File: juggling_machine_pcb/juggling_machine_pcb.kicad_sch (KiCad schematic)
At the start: 16 parts, among them J1 Conn_01x08, J10 Screw_Terminal_01x04, J11 Screw_Terminal_01x04, J2 Conn_01x08, J3 Conn_01x08, J4 Conn_01x08, J5 servo 1, J6 servo 2, J7 24v input, J8 5v input, J9 24v out for input to buck

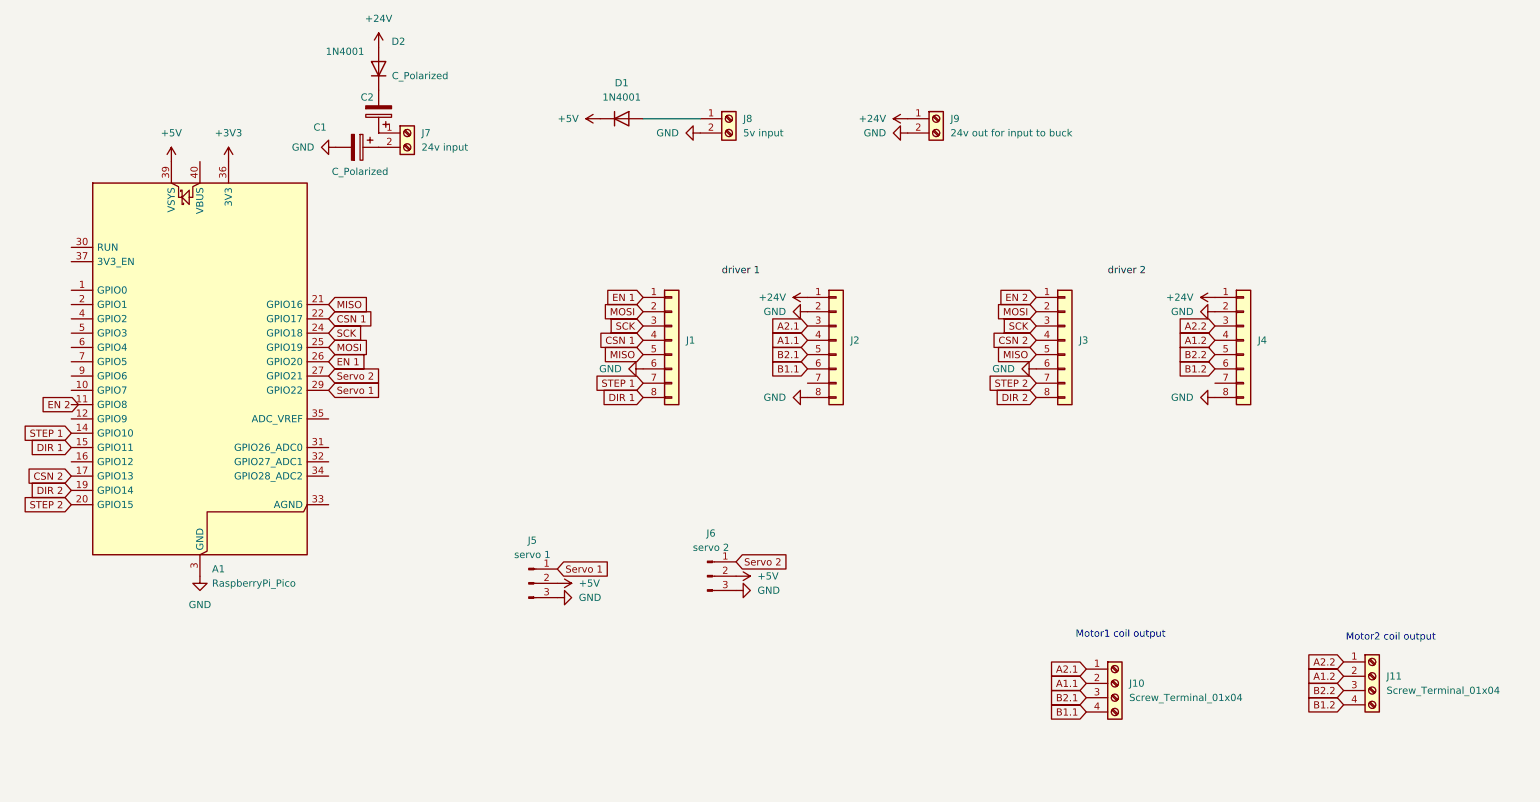
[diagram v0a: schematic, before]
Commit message: rerouted pcb with new motor driver footprint
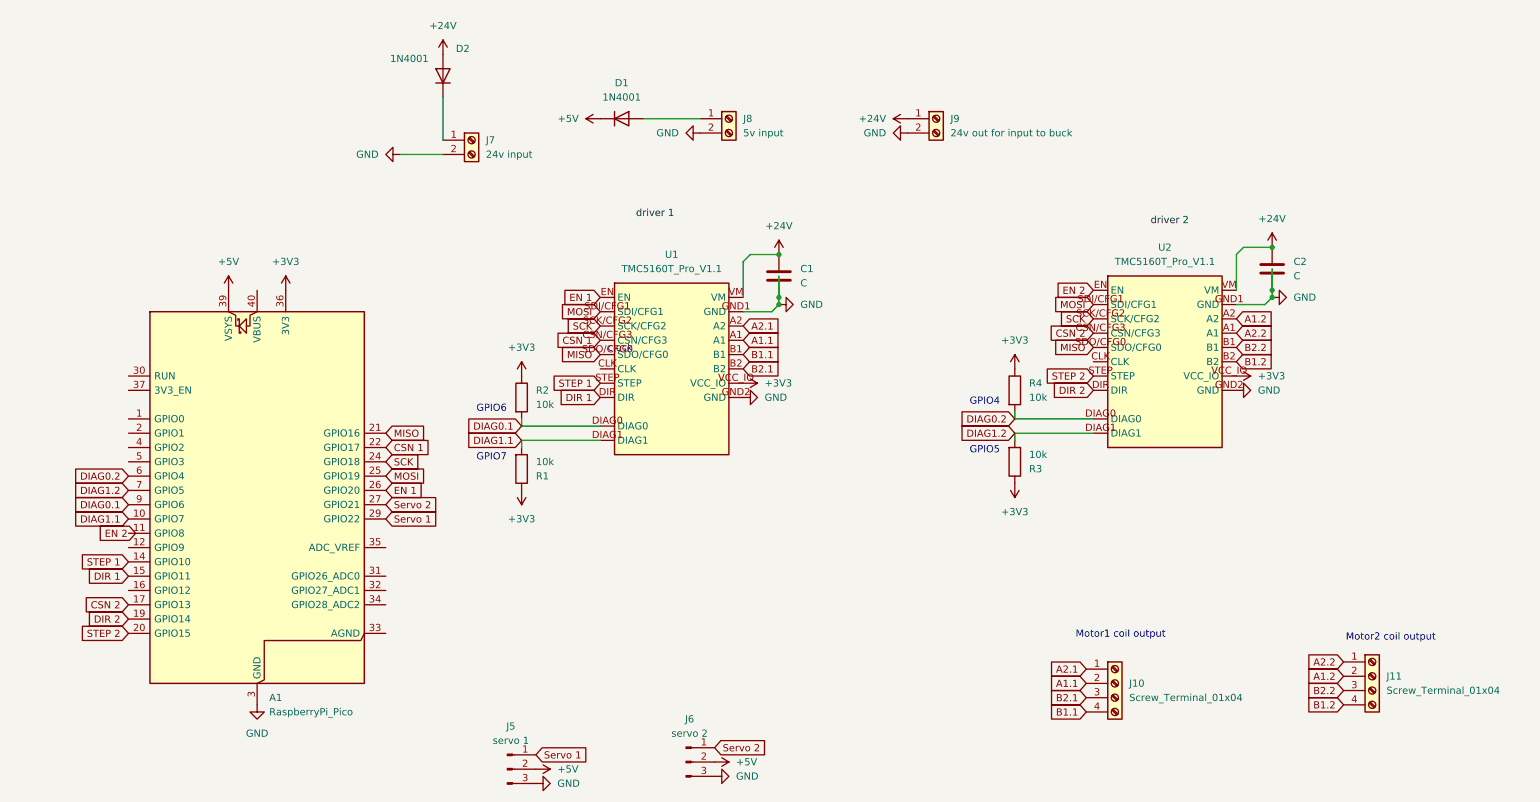
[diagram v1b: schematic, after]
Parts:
- removed C1, C2: C_Polarized, Capacitor_THT:CP_Radial_D8.0mm_P3.50mm, symbol Device:C_Polarized
- removed J1, J2, J3, J4: Conn_01x08, Connector_PinHeader_2.54mm:PinHeader_1x08_P2.54mm_Vertical, symbol Connector_Generic:Conn_01x08
- added C1, C2: C, Capacitor_THT:CP_Radial_D6.3mm_P2.50mm, symbol Device:C
- added R1, R2, R3, R4: 10k, Resistor_THT:R_Axial_DIN0204_L3.6mm_D1.6mm_P5.08mm_Horizontal, symbol Device:R
- added U1, U2: TMC5160T_Pro_V1.1, tmc driver:BTT_TMC5160T_Pro_V1.1, symbol TMC 5160:TMC5160T_Pro_V1.1
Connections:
- net +24V: now also C1.1, C2.1, U1.VM, U2.VM
- net +3V3: now also R1.1, R2.1, R3.1, R4.1, U1.VCC_IO, U2.VCC_IO
- net A1.1: now also U1.A1
- net A1.2: now also U2.A2
- net A2.1: now also U1.A2
- net A2.2: now also U2.A1
- net B1.1: now also U1.B1
- net B1.2: now also U2.B2
- net B2.1: now also U1.B2
- net B2.2: now also U2.B1
- net CSN 1: now also U1.CSN/CFG3
- net CSN 2: now also U2.CSN/CFG3
- net DIR 1: now also U1.DIR
- net DIR 2: now also U2.DIR
- net EN 1: now also U1.EN
- net EN 2: now also U2.EN
- net GND: now also J7.2 (Pin_2), C1.2, C2.2, U1.GND1 (GND), U1.GND2 (GND), U2.GND1 (GND), U2.GND2 (GND)
- net MISO: now also U1.SDO/CFG0, U2.SDO/CFG0
- net MOSI: now also U1.SDI/CFG1, U2.SDI/CFG1
- net SCK: now also U1.SCK/CFG2, U2.SCK/CFG2
- net STEP 1: now also U1.STEP
- net STEP 2: now also U2.STEP
- net DIAG1.1: now reaches A1.10 (GPIO7)
- net DIAG1.1: now also R1.2, U1.DIAG1
- net DIAG0.2: now reaches A1.6 (GPIO4)
- net DIAG0.2: now also R4.2, U2.DIAG0
- net DIAG1.2: now reaches A1.7 (GPIO5)
- net DIAG1.2: now also R3.2, U2.DIAG1
- net DIAG0.1: now reaches A1.9 (GPIO6)
- net DIAG0.1: now also R2.2, U1.DIAG0
- net at J7.1 (Pin_1): now also D2.1 (K)
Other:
- note added: "GPIO4"
- note added: "GPIO5"
- note added: "GPIO6"
- note added: "GPIO7"
- note added: "clock"
- moved on the sheet: A1, D2, J5, J6, J7
